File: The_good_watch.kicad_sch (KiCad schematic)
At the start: 51 parts, among them IC1 DW01A, J1 Main, J2 USB_C_Receptacle_USB2.0, J3 PROG, J4 Screen, J5 Button, J6 Conn_02x07_Counter_Clockwise, M1 Motor_DC, Q1 FS8205A, Q2 LP0404N3T5G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

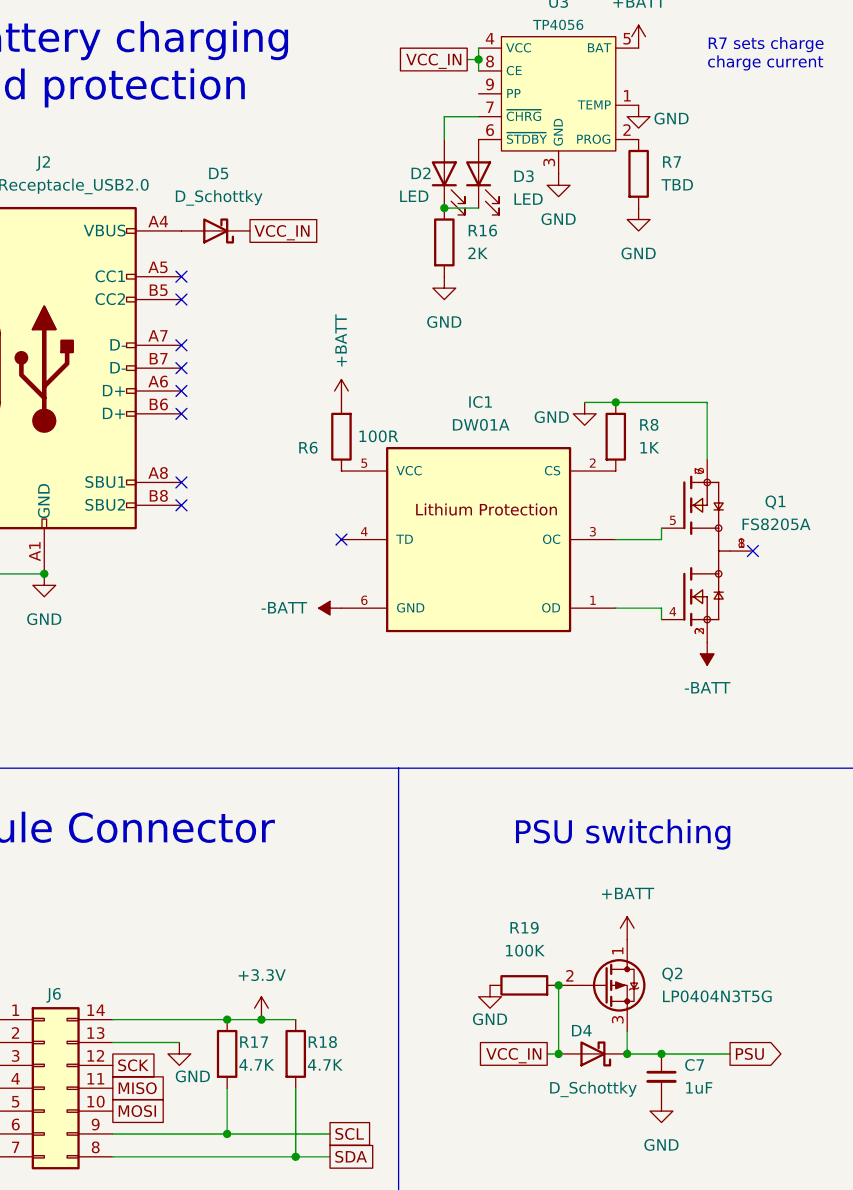
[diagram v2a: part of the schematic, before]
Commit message: Layout changes and fuse
Added fuse and fixed mosfet. Not changed on the pcb
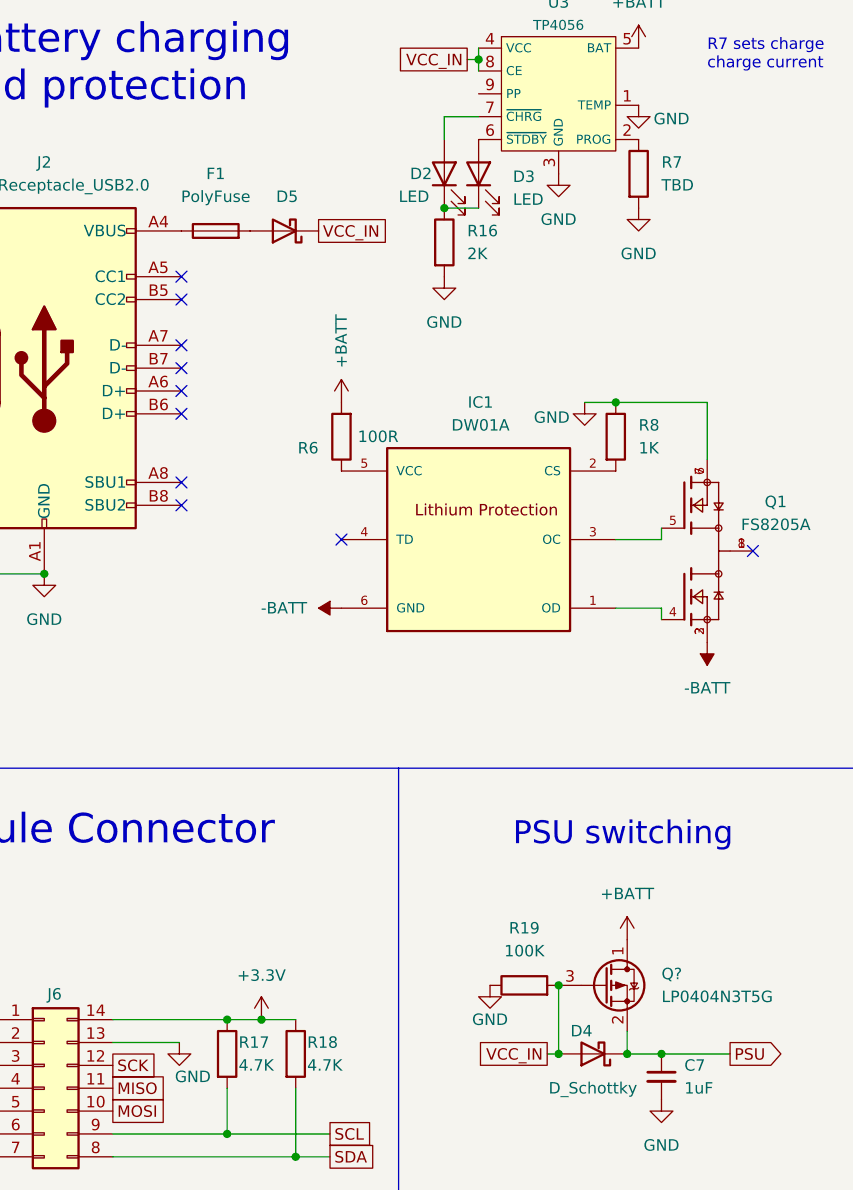
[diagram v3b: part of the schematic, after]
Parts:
- removed Q2: LP0404N3T5G, Package_TO_SOT_SMD:SOT-883, symbol Device:Q_PMOS_DGS
- added F1: PolyFuse, Fuse:Fuse_0603_1608Metric, symbol Device:Fuse
- added Q?: LP0404N3T5G, symbol Device:Q_PMOS_DSG
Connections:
- net +BATT: now also Q?.1 (D)
- net PSU: now also Q?.2 (S)
- net VCC_IN: now also Q?.3 (G)
- net at J2.A4 (VBUS), J2.A9 (VBUS), J2.B4 (VBUS)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: now also F1.1; no longer D5.2 (A)
- new net: D5.2 (A), F1.2
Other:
- moved on the sheet: D5
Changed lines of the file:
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@@
   (junction (at 251.46 133.35) (diameter 0) (color 0 0 0 0)
   )
-  (junction (at 251.46 125.73) (diameter 0) (color 0 0 0 0)
-  )
   (junction (at 118.11 57.15) (diameter 0) (color 0 0 0 0)
   )
@@
   (junction (at 88.2142 181.1274) (diameter 0) (color 0 0 0 0)
   )
+  (junction (at 251.46 125.73) (diameter 0) (color 0 0 0 0)
+  )
   (junction (at 59.69 138.43) (diameter 0) (color 0 0 0 0)
   )
@@
     (effects (font (size 3.27 3.27)) (justify left bottom))
   )
-  (global_label "VCC_IN" (shape passive) (at 217.17 41.91 0) (fields_autoplaced)
+  (global_label "VCC_IN" (shape passive) (at 224.79 41.91 0) (fields_autoplaced)
     (effects (font (size 1.27 1.27)) (justify left))
-    (property "Intersheet References" "${INTERSHEET_REFS}" (id 0) (at 226.1145 41.8306 0)
+    (property "Intersheet References" "${INTERSHEET_REFS}" (id 0) (at 233.7345 41.8306 0)
       (effects (font (size 1.27 1.27)) (justify left) hide)
     )
@@
     (pin "5")
   )
+  (symbol (lib_id "Device:Q_PMOS_DSG") (at 256.54 125.73 0) (unit 1)
+    (in_bom yes) (on_board yes) (fields_autoplaced)
+    (property "Reference" "Q?" (id 0) (at 262.89 124.4599 0)
+      (effects (font (size 1.27 1.27)) (justify left))
+    )
+    (property "Value" "LP0404N3T5G" (id 1) (at 262.89 126.9999 0)
+      (effects (font (size 1.27 1.27)) (justify left))
+    )
+    (property "Footprint" "" (id 2) (at 261.62 123.19 0)
+      (effects (font (size 1.27 1.27)) hide)
+    )
+    (property "Datasheet" "~" (id 3) (at 256.54 125.73 0)
+      (effects (font (size 1.27 1.27)) hide)
+    )
+    (pin "1")
+    (pin "2")
+    (pin "3")
+  )
   (symbol (lib_id "power:GND") (at 114.3 116.84 0) (unit 1)
     (in_bom yes) (on_board yes) (fields_autoplaced)
@@
     (pin "1")
   )
-  (symbol (lib_id "Device:Q_PMOS_DGS") (at 256.54 125.73 0) (unit 1)
+  (symbol (lib_id "Device:Fuse") (at 213.36 41.91 90) (unit 1)
     (in_bom yes) (on_board yes) (fields_autoplaced)
-    (property "Reference" "Q2" (id 0) (at 262.89 124.4599 0)
-      (effects (font (size 1.27 1.27)) (justify left))
-    )
-    (property "Value" "LP0404N3T5G" (id 1) (at 262.89 126.9999 0)
-      (effects (font (size 1.27 1.27)) (justify left))
-    )
-    (property "Footprint" "Package_TO_SOT_SMD:SOT-883" (id 2) (at 261.62 123.19 0)
+    (property "Reference" "F1" (id 0) (at 213.36 35.56 90))
+    (property "Value" "PolyFuse" (id 1) (at 213.36 38.1 90))
+    (property "Footprint" "Fuse:Fuse_0603_1608Metric" (id 2) (at 213.36 43.688 90)
       (effects (font (size 1.27 1.27)) hide)
     )
-    (property "Datasheet" "~" (id 3) (at 256.54 125.73 0)
+    (property "Datasheet" "~" (id 3) (at 213.36 41.91 0)
       (effects (font (size 1.27 1.27)) hide)
     )
     (pin "1")
     (pin "2")
-    (pin "3")
   )
   (symbol (lib_id "power:GND") (at 262.89 138.43 0) (unit 1)
@@
     (pin "6")
   )
-  (symbol (lib_id "Device:D_Schottky") (at 213.36 41.91 180) (unit 1)
+  (symbol (lib_id "Device:D_Schottky") (at 220.98 41.91 180) (unit 1)
     (in_bom yes) (on_board yes) (fields_autoplaced)
-    (property "Reference" "D5" (id 0) (at 213.6775 35.56 0))
-    (property "Value" "D_Schottky" (id 1) (at 213.6775 38.1 0))
-    (property "Footprint" "Diode_SMD:D_0603_1608Metric" (id 2) (at 213.36 41.91 0)
+    (property "Reference" "D5" (id 0) (at 221.2975 38.1 0))
+    (property "Value" "D_Schottky" (id 1) (at 221.2975 38.1 0)
       (effects (font (size 1.27 1.27)) hide)
     )
-    (property "Datasheet" "~" (id 3) (at 213.36 41.91 0)
+    (property "Footprint" "Diode_SMD:D_0603_1608Metric" (id 2) (at 220.98 41.91 0)
+      (effects (font (size 1.27 1.27)) hide)
+    )
+    (property "Datasheet" "~" (id 3) (at 220.98 41.91 0)
       (effects (font (size 1.27 1.27)) hide)
     )
@@
       (reference "D5") (unit 1) (value "D_Schottky") (footprint "Diode_SMD:D_0603_1608Metric")
     )
+    (path "/29a7e021-ede3-4fea-b3fa-52d502620992"
+      (reference "F1") (unit 1) (value "PolyFuse") (footprint "Fuse:Fuse_0603_1608Metric")
+    )
     (path "/94868651-0943-45d2-80cb-19057554eb97"
       (reference "IC1") (unit 1) (value "DW01A") (footprint "DW01A:SOT23-6")
@@
       (reference "Q1") (unit 1) (value "FS8205A") (footprint "FS8205A:SOP65P640X120-8N")
     )
-    (path "/27ef0546-932d-4d59-8105-a312b9106b63"
-      (reference "Q2") (unit 1) (value "LP0404N3T5G") (footprint "Package_TO_SOT_SMD:SOT-883")
+    (path "/25ce492d-5fce-4cd7-9136-dc23b5145044"
+      (reference "Q?") (unit 1) (value "LP0404N3T5G") (footprint "")
     )
     (path "/c224661f-9b65-4914-ba8e-266913ab43a5"
